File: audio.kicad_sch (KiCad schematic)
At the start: 24 parts, among them CN1 PJ-342, U8 PCM5122PW, U9 OPA1622IDRCR

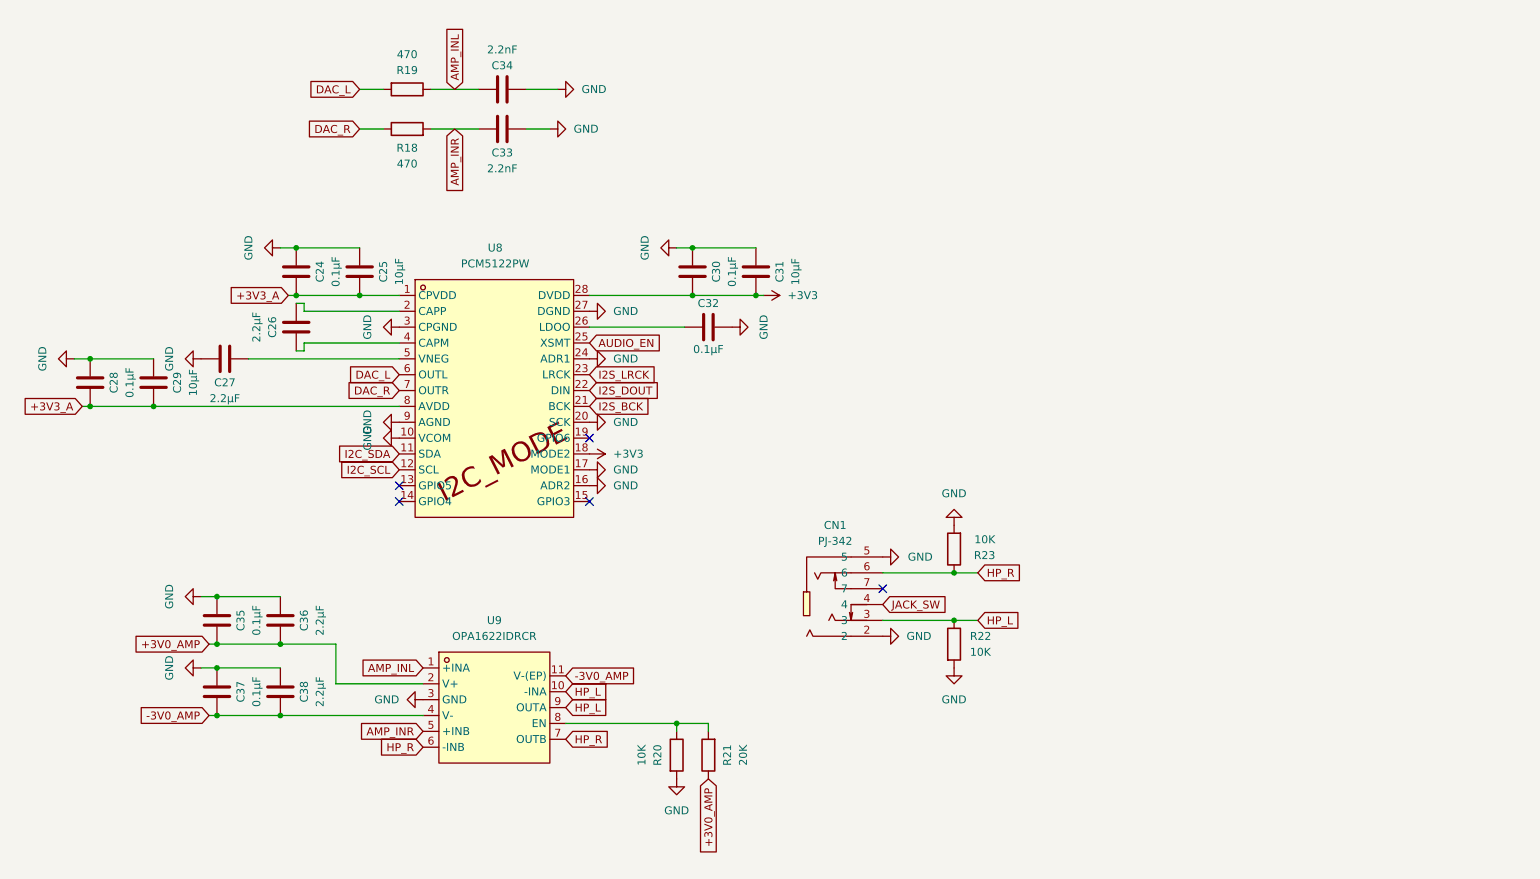
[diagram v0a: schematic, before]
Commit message: Schematic done
- sheet files renamed to English (usb, power, esp32, audio, io)
- final layout, annotation R1-R42 / C1-C43 / U1-U9 / J1-J4 / SW1-SW8
- all buttons are TS-1088, project R/C symbols, PWR_FLAGs
- connections.md replaces conexiuni.md (English, final references)
- final check on the KiCad netlist: 278/278 checks against connections.md
- status updated; firmware note: BQ25180 charge current defaults to ~10 mA

Co-Authored-By: Claude Opus 5.5 <noreply@anthropic.com>
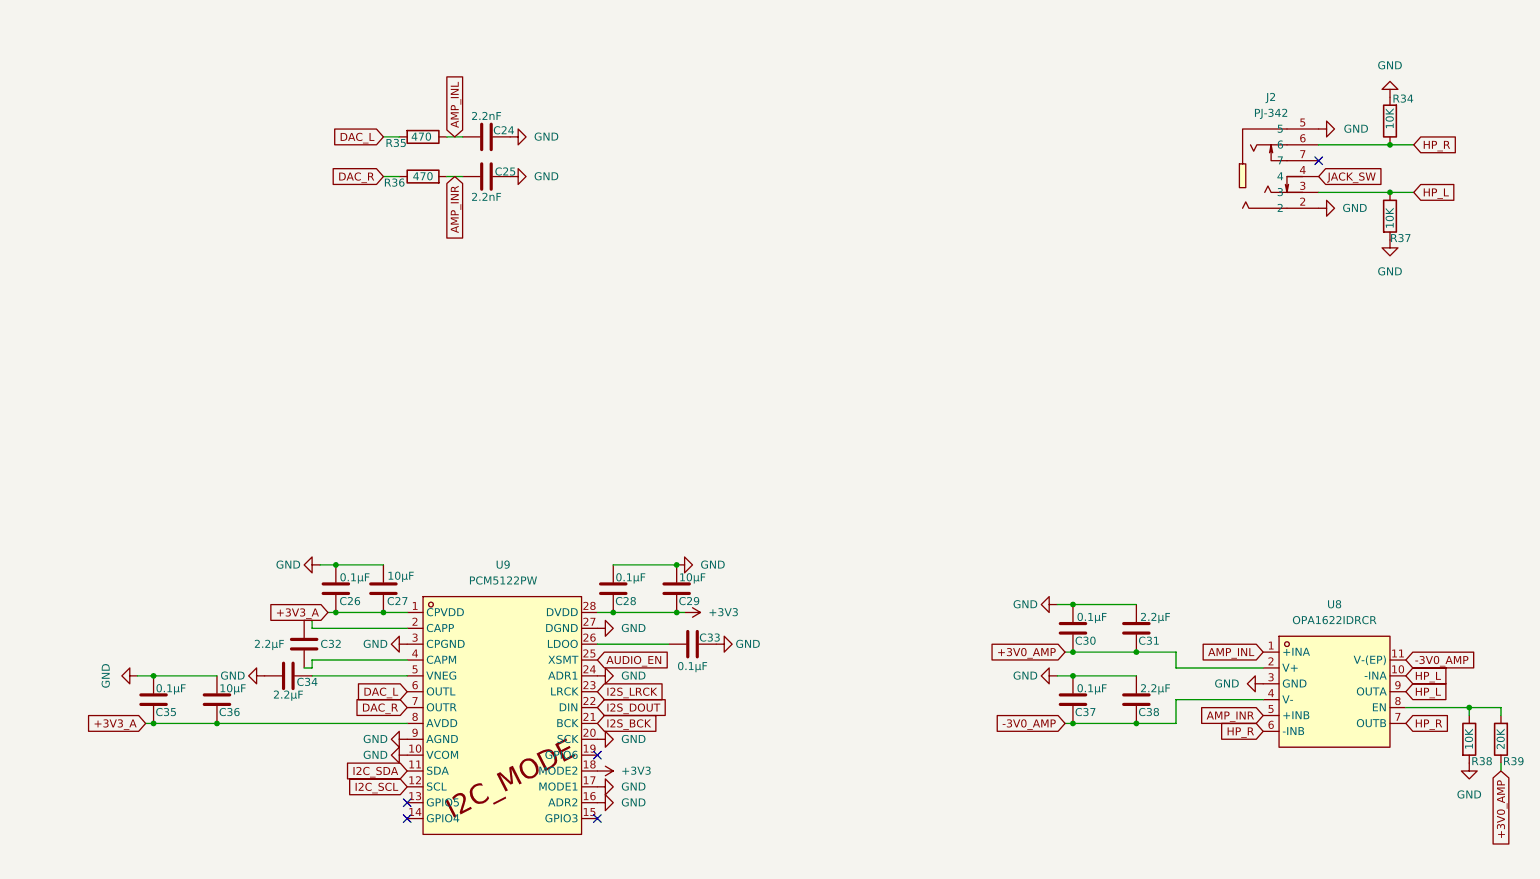
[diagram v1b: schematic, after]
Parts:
- R34: renamed from R23; symbol Device:R -> mp3_player:R
- R35: renamed from R19; symbol Device:R -> mp3_player:R
- R36: renamed from R18; symbol Device:R -> mp3_player:R
- R37: renamed from R22; symbol Device:R -> mp3_player:R
- R38: renamed from R20; symbol Device:R -> mp3_player:R
- R39: renamed from R21; symbol Device:R -> mp3_player:R
- renumbered C34 to C24, C33 to C25, C24 to C26, C25 to C27, C30 to C28, C31 to C29, C35 to C30, C36 to C31, C26 to C32, C32 to C33, C27 to C34, C28 to C35, C29 to C36, CN1 to J2, U9 to U8, U8 to U9
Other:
- moved on the sheet: C24, C25, C26, C27, C28, C29, C30, C31, C32, C33, C34, C35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

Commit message: Assign footprints and LCSC parts to passives, D2 and BT1
Thin-film 0.1% resistors in the audio path and rail dividers, C0G caps
in the DAC output filter, Samsung/Murata MLCCs with 0603/0805 cases for
bulk caps. Passive choices documented in mp3_player.md.

Co-Authored-By: Claude Opus 5.5 <noreply@anthropic.com>
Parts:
- C24, C25: footprint (none) -> Capacitor_SMD:C_0402_1005Metric; LCSC Part (none) -> C2987940
- C26, C28, C30, C33, C35, C37: footprint (none) -> Capacitor_SMD:C_0402_1005Metric; LCSC Part (none) -> C1525
- C27, C29, C36: footprint (none) -> Capacitor_SMD:C_0603_1608Metric; LCSC Part (none) -> C19702
- C31, C32, C34, C38: footprint (none) -> Capacitor_SMD:C_0603_1608Metric; LCSC Part (none) -> C23630
- R34, R37, R38: footprint (none) -> Resistor_SMD:R_0402_1005Metric; LCSC Part (none) -> C190095
- R35, R36: footprint (none) -> Resistor_SMD:R_0402_1005Metric; LCSC Part (none) -> C852799
- R39: footprint (none) -> Resistor_SMD:R_0402_1005Metric; LCSC Part (none) -> C705630

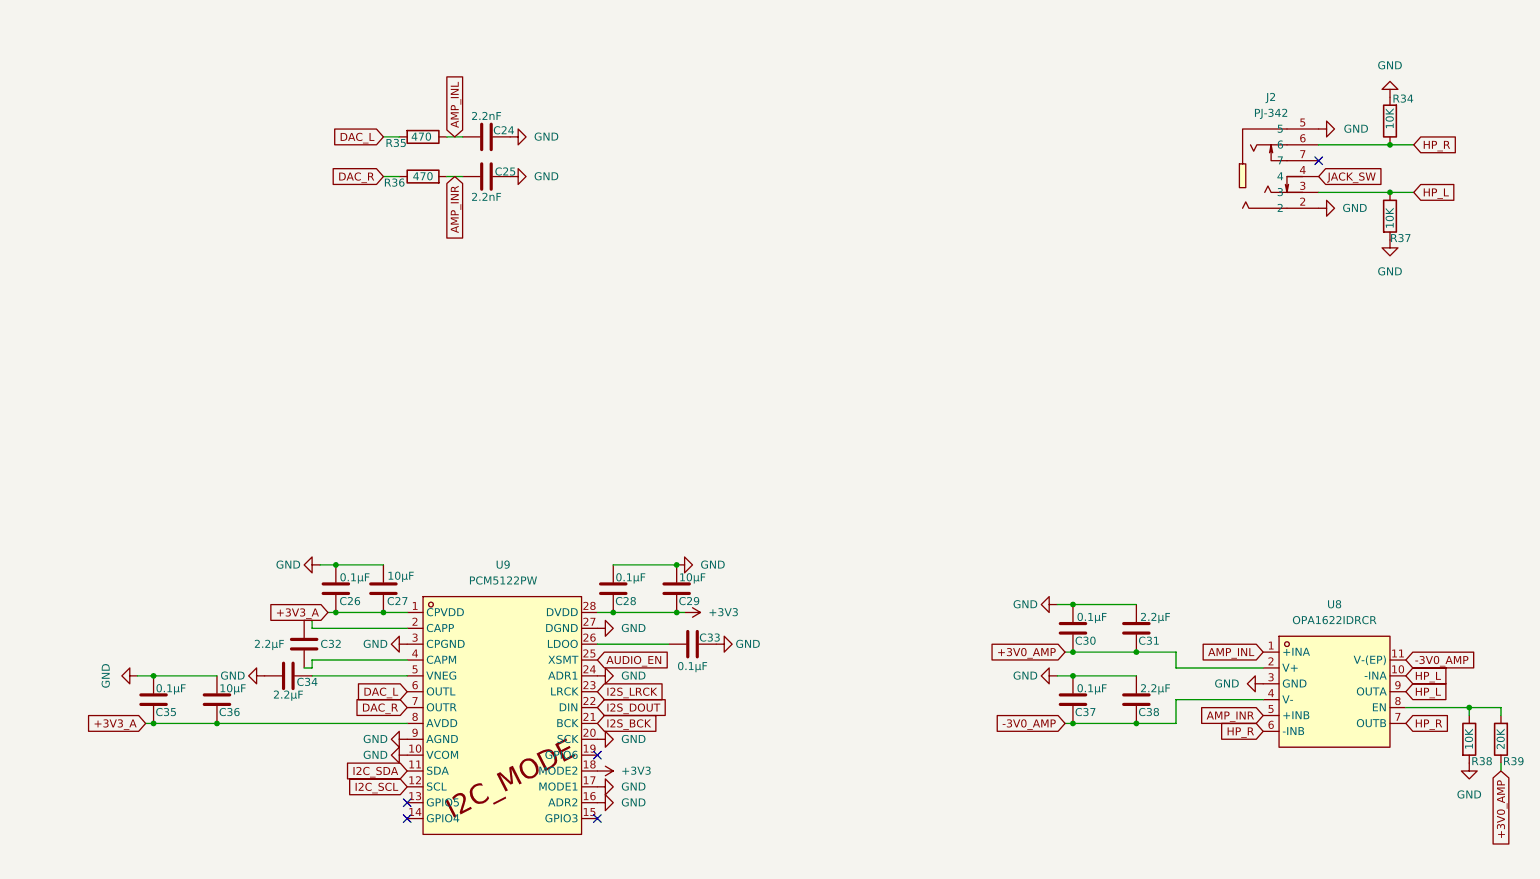
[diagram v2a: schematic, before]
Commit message: Fix ERC and document enclosure concept
- ERC clean: power flags moved onto real nets, USBLC6 pin types,
  Unspecified pins allowed in the pin conflict map, off-grid wires aligned
- mp3_player.md: enclosure section (anodized aluminium v1, titanium v2,
  printed click wheel and antenna cap, build123d workflow)
- ignore the build123d venv

Co-Authored-By: Claude Opus 5.5 <noreply@anthropic.com>
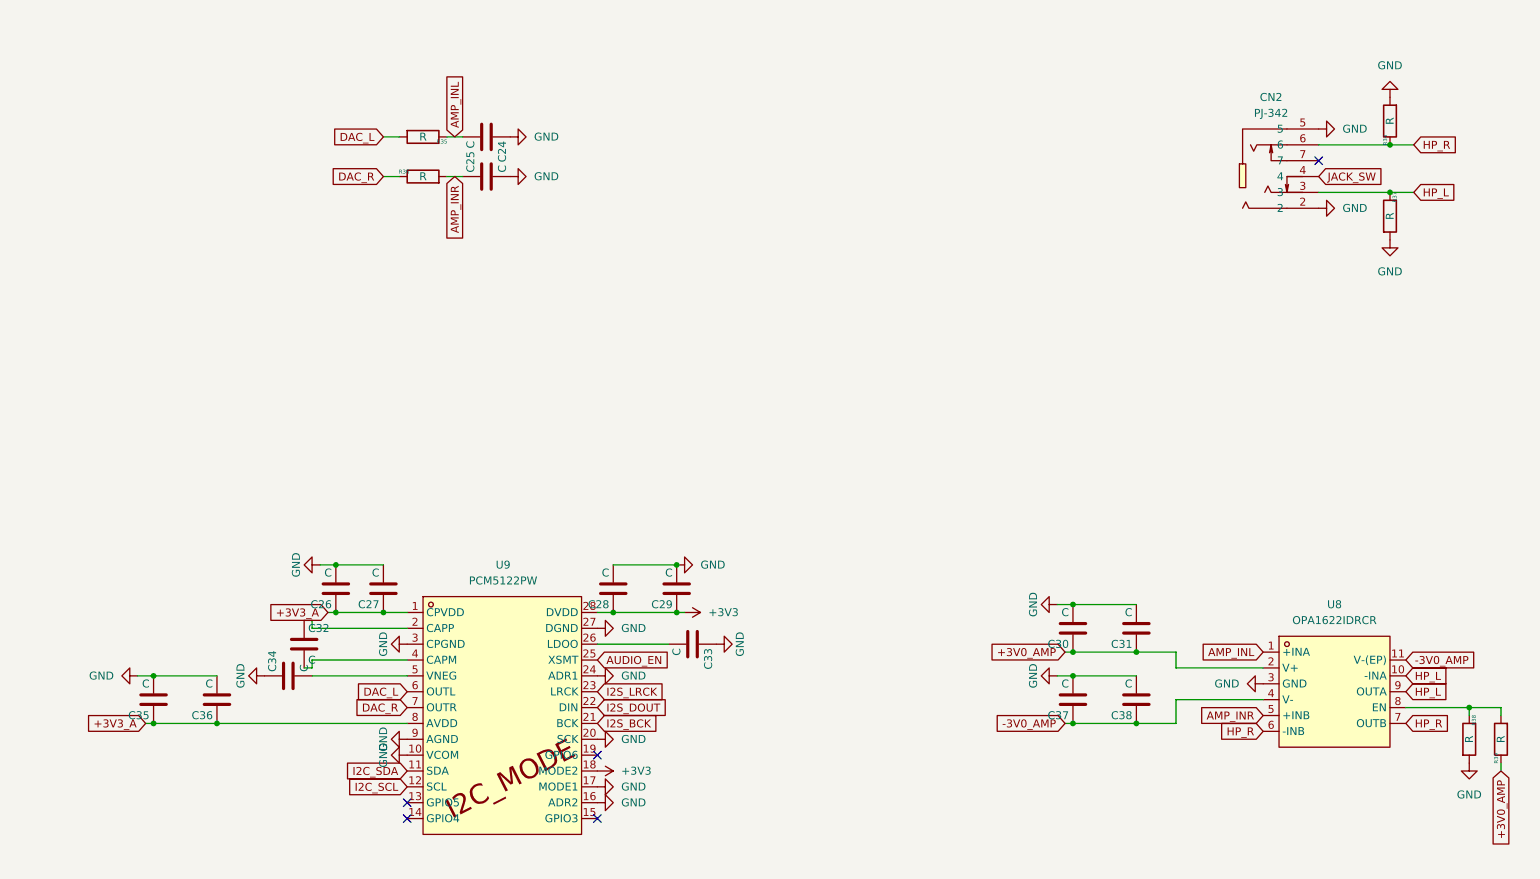
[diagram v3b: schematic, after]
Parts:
- C24, C25: value 2.2nF -> C
- C26, C28, C30, C33, C35, C37: value 0.1µF -> C
- C27, C29, C36: value 10µF -> C
- C31, C32, C34, C38: value 2.2µF -> C
- R34, R37, R38: value 10K -> R
- R35, R36: value 470 -> R
- R39: value 20K -> R
- renumbered J2 to CN2

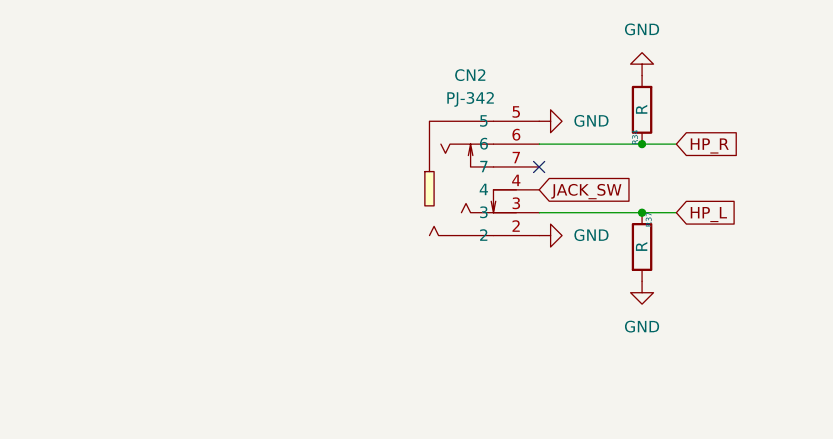
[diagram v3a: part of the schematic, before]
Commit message: Schematic and parts for enclosure B
- jack PJ-342C CB (TRRS, sinking) as CN1, HP-DET on JACK_SW, MIC to GND,
  100nF on JACK_DET (detect is now active low)
- USB-C TYPE-C 16P CB0.8 073 (sinking, 0.8 mm board) as USB1
- BT1 on JST SH SM02B-SRSS-TB, click wheel on TS-1187B-B (0.75 mm),
  power on EVQP7J01P side switch
- new footprints/3D models in lib; switch and JST SH footprints renumbered
  so the existing 2-pin symbols fit
- enclosure: power key on the right side, level with the display
- docs: connections.md, code.md and BOM updated

ERC: 0 errors, 0 warnings.

Co-Authored-By: Claude Opus 5.5 <noreply@anthropic.com>
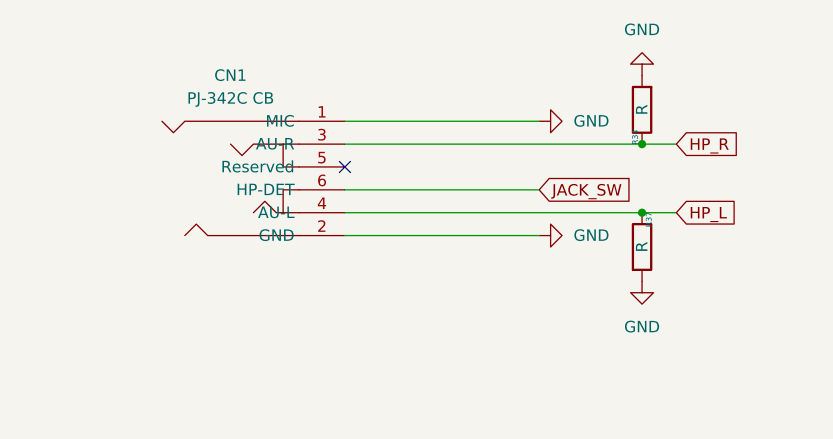
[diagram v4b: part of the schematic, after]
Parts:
- removed CN2: PJ-342, mp3_player:AUDIO-SMD_PJ-342_C668606, symbol mp3_player:PJ-342
- added CN1: PJ-342C CB, mp3_player:AUDIO-SMD_HX-PJ-342C, symbol mp3_player:PJ-342CCB
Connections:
- net GND: now also CN1.1 (MIC), CN1.2 (GND)
- net HP_L: now also CN1.4 (AU-L)
- net HP_R: now also CN1.3 (AU-R)
- net JACK_SW: now also CN1.6 (HP-DET)
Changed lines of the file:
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@@
 	)
 	(no_connect
-		(at 228.6 46.99)
+		(at 207.01 46.99)
 	)
 	(no_connect
@@
 	(wire
 		(pts
-			(xy 240.03 44.45) (xy 243.84 44.45)
-		)
-		(stroke
-			(width 0)
-			(type default)
-		)
-	)
-	(wire
-		(pts
-			(xy 243.84 52.07) (xy 240.03 52.07)
+			(xy 207.01 49.53) (xy 228.6 49.53)
 		)
 		(stroke
@@
 	(wire
 		(pts
-			(xy 205.74 125.73) (xy 199.39 125.73)
+			(xy 207.01 44.45) (xy 243.84 44.45)
 		)
 		(stroke
@@
 	(wire
 		(pts
-			(xy 205.74 137.16) (xy 205.74 133.35)
+			(xy 205.74 125.73) (xy 199.39 125.73)
 		)
 		(stroke
@@
 	(wire
 		(pts
-			(xy 228.6 44.45) (xy 240.03 44.45)
+			(xy 205.74 137.16) (xy 205.74 133.35)
 		)
 		(stroke
@@
 	(wire
 		(pts
-			(xy 240.03 52.07) (xy 228.6 52.07)
+			(xy 67.31 120.65) (xy 66.04 120.65)
 		)
 		(stroke
@@
 	(wire
 		(pts
-			(xy 67.31 120.65) (xy 66.04 120.65)
+			(xy 207.01 41.91) (xy 228.6 41.91)
 		)
 		(stroke
@@
 	(wire
 		(pts
+			(xy 207.01 52.07) (xy 243.84 52.07)
+		)
+		(stroke
+			(width 0)
+			(type default)
+		)
+	)
+	(wire
+		(pts
 			(xy 252.73 135.89) (xy 252.73 134.62)
 		)
@@
 		)
 	)
+	(wire
+		(pts
+			(xy 207.01 54.61) (xy 228.6 54.61)
+		)
+		(stroke
+			(width 0)
+			(type default)
+		)
+	)
 	(global_label "HP_R"
 		(shape input)
@@
 	)
 	(symbol
-		(lib_id "mp3_player:PJ-342")
-		(at 222.25 46.99 0)
-		(unit 1)
-		(body_style 1)
-		(exclude_from_sim no)
-		(in_bom yes)
-		(on_board yes)
-		(in_pos_files yes)
-		(dnp no)
-		(fields_autoplaced yes)
-		(property "Reference" "CN2"
-			(at 220.98 36.83 0)
-			(show_name no)
-			(do_not_autoplace no)
-			(effects
-				(font
-					(size 1.27 1.27)
-				)
-			)
-		)
-		(property "Value" "PJ-342"
-			(at 220.98 39.37 0)
-			(show_name no)
-			(do_not_autoplace no)
-			(effects
-				(font
-					(size 1.27 1.27)
-				)
-			)
-		)
-		(property "Footprint" "mp3_player:AUDIO-SMD_PJ-342_C668606"
-			(at 222.25 62.23 0)
-			(hide yes)
-			(show_name no)
-			(do_not_autoplace no)
-			(effects
-				(font
-					(size 1.27 1.27)
-				)
-			)
-		)
-		(property "Datasheet" "https://lcsc.com/product-detail/Audio-Video-Connectors_SHOU-HAN-PJ-342_C668606.html"
-			(at 222.25 64.77 0)
-			(hide yes)
-			(show_name no)
-			(do_not_autoplace no)
-			(effects
-				(font
-					(size 1.27 1.27)
-				)
-			)
-		)
-		(property "Description" ""
-			(at 222.25 46.99 0)
-			(hide yes)
-			(show_name no)
-			(do_not_autoplace no)
-			(effects
-				(font
-					(size 1.27 1.27)
-				)
-			)
-		)
-		(property "Manufacturer" "SHOU HAN(首韩)"
-			(at 222.25 67.31 0)
-			(hide yes)
-			(show_name no)
-			(do_not_autoplace no)
-			(effects
-				(font
-					(size 1.27 1.27)
-				)
-			)
-		)
-		(property "MPN" "PJ-342"
-			(at 222.25 69.85 0)
-			(hide yes)
-			(show_name no)
-			(do_not_autoplace no)
-			(effects
-				(font
-					(size 1.27 1.27)
-				)
-			)
-		)
-		(property "LCSC Part" "C668606"
-			(at 222.25 72.39 0)
-			(hide yes)
-			(show_name no)
-			(do_not_autoplace no)
-			(effects
-				(font
-					(size 1.27 1.27)
-				)
-			)
-		)
-		(pin "4"
-		)
-		(pin "5"
-		)
-		(pin "7"
-		)
-		(pin "6"
-		)
-		(pin "3"
-		)
-		(pin "2"
-		)
-		(instances
-			(project "mp3_player"
-				(path "/c6422f90-0327-4136-a608-1204883e57cc"
-					(reference "CN2")
-					(unit 1)
-				)
-			)
-		)
-	)
-	(symbol
 		(lib_id "mp3_player:R")
 		(at 85.09 43.18 270)
@@
 					(unit 1)
 				)
+			)
+		)
+	)
+	(symbol
+		(lib_id "mp3_player:PJ-342CCB")
+		(at 196.85 46.99 0)
+		(unit 1)
+		(body_style 1)
+		(exclude_from_sim no)
+		(in_bom yes)
+		(on_board yes)
+		(in_pos_files yes)
+		(dnp no)
+		(fields_autoplaced yes)
+		(property "Reference" "CN1"
+			(at 194.31 36.83 0)
+			(show_name no)
+			(do_not_autoplace no)
+			(effects
+				(font
+					(size 1.27 1.27)
+				)
+			)
+		)
+		(property "Value" "PJ-342C CB"
+			(at 194.31 39.37 0)
+			(show_name no)
+			(do_not_autoplace no)
+			(effects
+				(font
+					(size 1.27 1.27)
+				)
+			)
+		)
+		(property "Footprint" "mp3_player:AUDIO-SMD_HX-PJ-342C"
+			(at 196.85 62.23 0)
+			(hide yes)
+			(show_name no)
+			(do_not_autoplace no)
+			(effects
+				(font
+					(size 1.27 1.27)
+				)
+			)
+		)
+		(property "Datasheet" "https://www.lcsc.com/datasheet/C49287245.pdf"
+			(at 196.85 64.77 0)
+			(hide yes)
+			(show_name no)
+			(do_not_autoplace no)
+			(effects
+				(font
+					(size 1.27 1.27)
+				)
+			)
+		)
+		(property "Description" ""
+			(at 196.85 46.99 0)
+			(hide yes)
+			(show_name no)
+			(do_not_autoplace no)
+			(effects
+				(font
+					(size 1.27 1.27)
+				)
+			)
+		)
+		(property "Manufacturer" "SHOU HAN(首韩)"
+			(at 196.85 67.31 0)
+			(hide yes)
+			(show_name no)
+			(do_not_autoplace no)
+			(effects
+				(font
+					(size 1.27 1.27)
+				)
+			)
+		)
+		(property "MPN" "PJ-342C CB"
+			(at 196.85 69.85 0)
+			(hide yes)
+			(show_name no)
+			(do_not_autoplace no)
+			(effects
+				(font
+					(size 1.27 1.27)
+				)
+			)
+		)
+		(property "LCSC Part" "C49287245"
+			(at 196.85 72.39 0)
+			(hide yes)
+			(show_name no)
+			(do_not_autoplace no)
+			(effects
+				(font
+					(size 1.27 1.27)
+				)
+			)
+		)
+		(pin "5"
+		)
+		(pin "6"
+		)
+		(pin "4"
+		)
+		(pin "1"
+		)
+		(pin "2"
+		)
+		(pin "3"
+		)
+		(instances
+			(project "mp3_player"
+				(path "/c6422f90-0327-4136-a608-1204883e57cc"
+					(reference "CN1")
+					(unit 1)
+				)
